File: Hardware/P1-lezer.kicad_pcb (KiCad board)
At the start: 2 copper layers, 70 x 30 mm, 13 parts, among them J1 RJ12, M2.5 MountingHole_2.7mm_M2.5_ISO73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, Q1 BC547, U1 WeMos_D1_mini, U2 TIL111

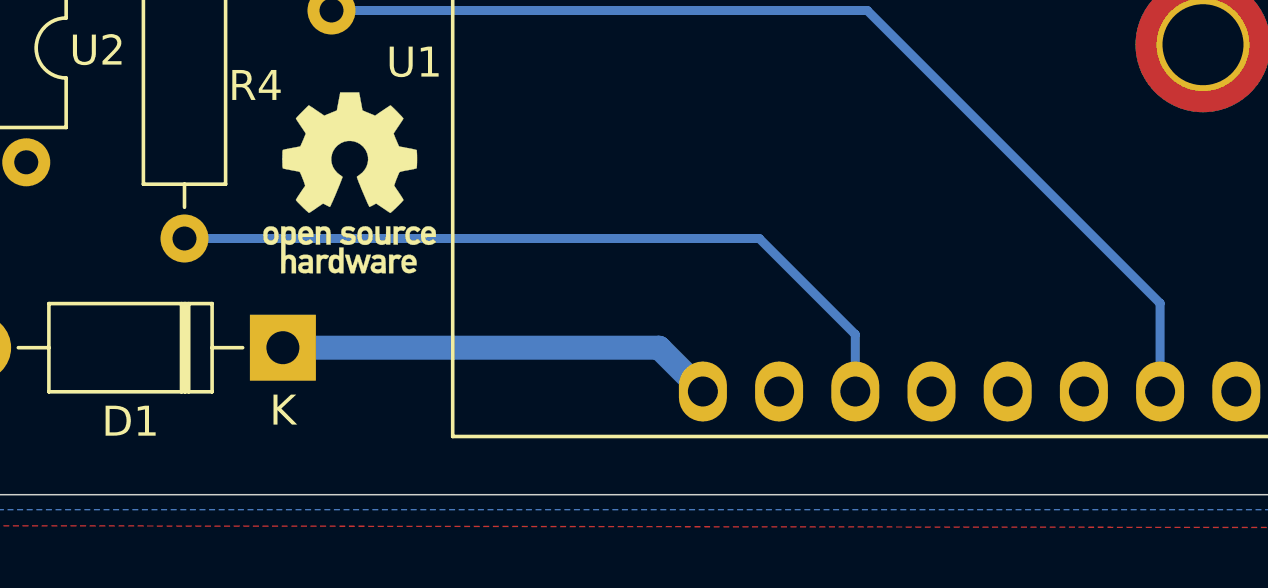
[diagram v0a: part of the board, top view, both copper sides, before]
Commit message: Moved request line to D1 and rerouted the board to match this change.
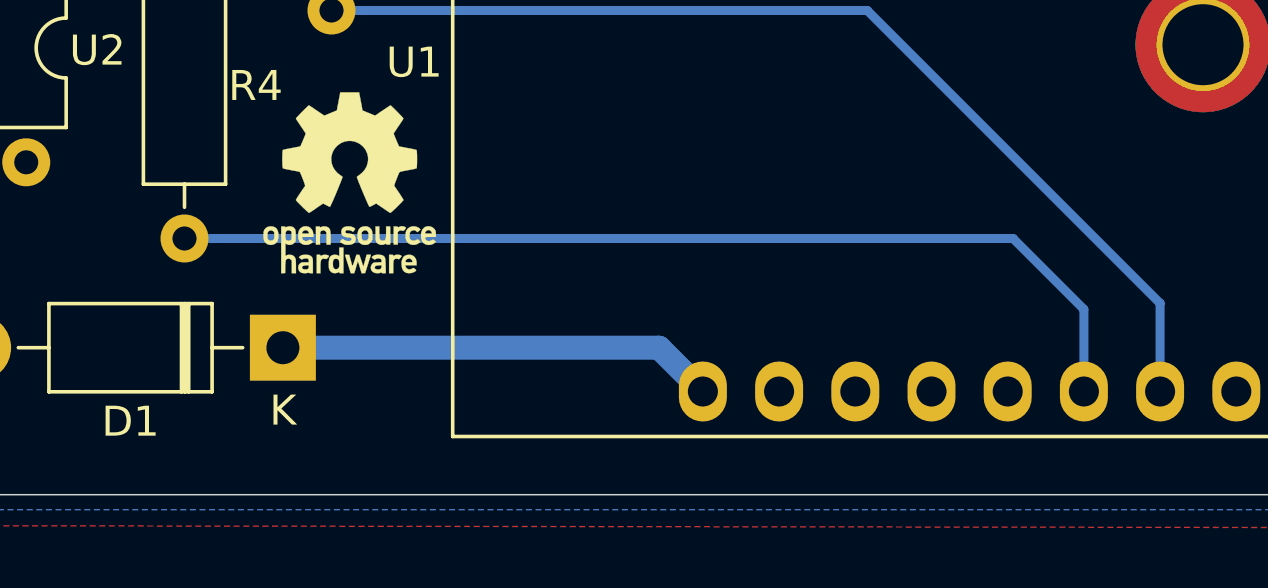
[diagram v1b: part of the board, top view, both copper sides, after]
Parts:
- R4: value 200 -> 220
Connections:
- U1 pad 11: Req -> unconnected-(U1-D4-Pad11)
- U1 pad 14: unconnected-(U1-SCL/D1-Pad14) -> Req
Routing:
- net Req: track 25.6 -> 33.7 mm
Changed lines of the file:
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@@
 	(net 15 "unconnected-(U1-D0-Pad3)")
 	(net 16 "unconnected-(U1-A0-Pad2)")
-	(net 17 "unconnected-(U1-SCL{slash}D1-Pad14)")
-	(net 18 "unconnected-(U1-SCK{slash}D5-Pad4)")
-	(net 19 "unconnected-(U1-CS{slash}D8-Pad7)")
-	(net 20 "unconnected-(U1-SDA{slash}D2-Pad13)")
-	(net 21 "unconnected-(J1-Pad4)")
-	(net 22 "unconnected-(U2-NC-Pad3)")
-	(net 23 "unconnected-(U2-Pad6)")
-	(net 24 "Net-(D1-K)")
+	(net 17 "unconnected-(U1-D4-Pad11)")
+	(net 18 "unconnected-(U1-CS{slash}D8-Pad7)")
+	(net 19 "unconnected-(U1-SDA{slash}D2-Pad13)")
+	(net 20 "unconnected-(J1-Pad4)")
+	(net 21 "unconnected-(U2-NC-Pad3)")
+	(net 22 "unconnected-(U2-Pad6)")
+	(net 23 "Net-(D1-K)")
+	(net 24 "unconnected-(U1-SCK{slash}D5-Pad4)")
 	(footprint "Symbol:OSHW-Logo_5.7x6mm_SilkScreen"
 		(layer "F.Cu")
@@
 			)
 		)
-		(property "Value" "200"
+		(property "Value" "220"
 			(at 5.08 2.37 90)
 			(layer "F.Fab")
@@
 			)
 		)
+		(property "Untitled Field" ""
+			(at 0 0 -90)
+			(unlocked yes)
+			(layer "F.Fab")
+			(hide yes)
+			(effects
+				(font
+					(size 1 1)
+					(thickness 0.15)
+				)
+			)
+		)
 		(property ki_fp_filters "R_*")
 		(sheetname "Root")
@@
 			(layers "*.Cu" "*.Mask")
 			(remove_unused_layers no)
-			(net 18 "unconnected-(U1-SCK{slash}D5-Pad4)")
+			(net 24 "unconnected-(U1-SCK{slash}D5-Pad4)")
 			(pinfunction "SCK/D5")
 			(pintype "bidirectional+no_connect")
@@
 			(layers "*.Cu" "*.Mask")
 			(remove_unused_layers no)
-			(net 19 "unconnected-(U1-CS{slash}D8-Pad7)")
+			(net 18 "unconnected-(U1-CS{slash}D8-Pad7)")
 			(pinfunction "CS/D8")
 			(pintype "bidirectional+no_connect")
@@
 			(layers "*.Cu" "*.Mask")
 			(remove_unused_layers no)
-			(net 24 "Net-(D1-K)")
+			(net 23 "Net-(D1-K)")
 			(pinfunction "5V")
 			(pintype "power_in")
@@
 			(layers "*.Cu" "*.Mask")
 			(remove_unused_layers no)
-			(net 7 "Req")
+			(net 17 "unconnected-(U1-D4-Pad11)")
 			(pinfunction "D4")
-			(pintype "bidirectional")
+			(pintype "bidirectional+no_connect")
 		)
 		(pad "12" thru_hole oval
@@
 			(layers "*.Cu" "*.Mask")
 			(remove_unused_layers no)
-			(net 20 "unconnected-(U1-SDA{slash}D2-Pad13)")
+			(net 19 "unconnected-(U1-SDA{slash}D2-Pad13)")
 			(pinfunction "SDA/D2")
 			(pintype "bidirectional+no_connect")
@@
 			(layers "*.Cu" "*.Mask")
 			(remove_unused_layers no)
-			(net 17 "unconnected-(U1-SCL{slash}D1-Pad14)")
+			(net 7 "Req")
 			(pinfunction "SCL/D1")
-			(pintype "bidirectional+no_connect")
+			(pintype "bidirectional")
 		)
 		(pad "15" thru_hole oval
@@
 			(layers "*.Cu" "*.Mask")
 			(remove_unused_layers no)
-			(net 21 "unconnected-(J1-Pad4)")
+			(net 20 "unconnected-(J1-Pad4)")
 			(pintype "passive+no_connect")
 		)
@@
 			(layers "*.Cu" "*.Mask")
 			(remove_unused_layers no)
-			(net 22 "unconnected-(U2-NC-Pad3)")
+			(net 21 "unconnected-(U2-NC-Pad3)")
 			(pinfunction "NC")
 			(pintype "no_connect")
@@
 			(layers "*.Cu" "*.Mask")
 			(remove_unused_layers no)
-			(net 23 "unconnected-(U2-Pad6)")
+			(net 22 "unconnected-(U2-Pad6)")
 			(pintype "passive+no_connect")
 		)
@@
 			(layers "*.Cu" "*.Mask")
 			(remove_unused_layers no)
-			(net 24 "Net-(D1-K)")
+			(net 23 "Net-(D1-K)")
 			(pinfunction "K")
 			(pintype "passive")
@@
 	)
 	(segment
-		(start 117.36 88.46)
-		(end 98.2 88.46)
+		(start 125.82 88.46)
+		(end 128.18 90.82)
 		(width 0.3)
 		(layer "B.Cu")
@@
 	)
 	(segment
-		(start 120.56 91.66)
-		(end 117.36 88.46)
+		(start 128.18 90.82)
+		(end 128.18 93.56)
 		(width 0.3)
 		(layer "B.Cu")
@@
 	)
 	(segment
-		(start 120.56 93.56)
-		(end 120.56 91.66)
+		(start 98.2 88.46)
+		(end 125.82 88.46)
 		(width 0.3)
 		(layer "B.Cu")
@@
 		(width 0.8)
 		(layer "B.Cu")
-		(net 24)
+		(net 23)
 	)
 	(segment
@@
 		(width 0.8)
 		(layer "B.Cu")
-		(net 24)
+		(net 23)
 	)
 	(zone

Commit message: Regenerated gerbers
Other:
- board text added: "Rev.B"
- board text removed: "Rev.A"
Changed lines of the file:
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@@
 		)
 	)
-	(gr_text "Rev.A"
+	(gr_text "Rev.B"
 		(at 75.2 94.6 0)
 		(layer "F.SilkS")

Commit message: Optocoupler aangepast naar CNY17-1
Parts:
- U2: value TIL111 -> CNY17-1
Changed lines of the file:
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@@
 				(font
 					(size 1.27 1.27)
+					(thickness 0.15)
 				)
 			)
@@
 				(font
 					(size 1.27 1.27)
+					(thickness 0.15)
 				)
 			)
@@
 				(font
 					(size 1.27 1.27)
+					(thickness 0.15)
 				)
 			)
@@
 				(font
 					(size 1.27 1.27)
+					(thickness 0.15)
 				)
 			)
@@
 				(font
 					(size 1.27 1.27)
+					(thickness 0.15)
 				)
 			)
@@
 				(font
 					(size 1.27 1.27)
+					(thickness 0.15)
 				)
 			)
@@
 				(font
 					(size 1.27 1.27)
+					(thickness 0.15)
 				)
 			)
@@
 				(font
 					(size 1.27 1.27)
+					(thickness 0.15)
 				)
 			)
@@
 				(font
 					(size 1.27 1.27)
+					(thickness 0.15)
 				)
 			)
@@
 				(font
 					(size 1.27 1.27)
+					(thickness 0.15)
 				)
 			)
@@
 				(font
 					(size 1.27 1.27)
+					(thickness 0.15)
 				)
 			)
@@
 				(font
 					(size 1.27 1.27)
+					(thickness 0.15)
 				)
 			)
@@
 				(font
 					(size 1.27 1.27)
+					(thickness 0.15)
 				)
 			)
@@
 				(font
 					(size 1.27 1.27)
+					(thickness 0.15)
 				)
 			)
@@
 				(font
 					(size 1.27 1.27)
+					(thickness 0.15)
 				)
 			)
@@
 				(font
 					(size 1.27 1.27)
+					(thickness 0.15)
 				)
 			)
@@
 				(font
 					(size 1.27 1.27)
+					(thickness 0.15)
 				)
 			)
@@
 				(font
 					(size 1.27 1.27)
+					(thickness 0.15)
 				)
 			)
@@
 				(font
 					(size 1.27 1.27)
+					(thickness 0.15)
 				)
 			)
@@
 				(font
 					(size 1.27 1.27)
+					(thickness 0.15)
 				)
 			)
@@
 				(font
 					(size 1.27 1.27)
+					(thickness 0.15)
 				)
 			)
@@
 				(font
 					(size 1.27 1.27)
+					(thickness 0.15)
 				)
 			)
@@
 				(font
 					(size 1.27 1.27)
+					(thickness 0.15)
 				)
 			)
@@
 				(font
 					(size 1.27 1.27)
+					(thickness 0.15)
 				)
 			)
@@
 				(font
 					(size 1.27 1.27)
+					(thickness 0.15)
 				)
 			)
@@
 				(font
 					(size 1.27 1.27)
+					(thickness 0.15)
 				)
 			)
@@
 				(font
 					(size 1.27 1.27)
+					(thickness 0.15)
 				)
 			)
@@
 			)
 		)
-		(property "Value" "TIL111"
+		(property "Value" "CNY17-1"
 			(at 3.81 7.41 90)
 			(layer "F.Fab")
@@
 				(font
 					(size 1.27 1.27)
+					(thickness 0.15)
 				)
 			)
 		)
-		(property "Datasheet" "https://www.egr.msu.edu/eceshop/Parts_Inventory/datasheets/til111.pdf"
+		(property "Datasheet" "http://www.vishay.com/docs/83606/cny17.pdf"
 			(at 0 0 -90)
 			(unlocked yes)
@@
 				(font
 					(size 1.27 1.27)
+					(thickness 0.15)
 				)
 			)
 		)
-		(property "Description" "DC Optocoupler, Phototransistor NPN, DIP6"
+		(property "Description" "DC Optocoupler Base Connected, Vce 70V, CTR 40-80%, Viso 5000V (RMS), DIP6"
 			(at 0 0 -90)
 			(unlocked yes)
@@
 				(font
 					(size 1.27 1.27)
+					(thickness 0.15)
 				)
 			)
 		)
-		(property ki_fp_filters "DIP*W7.62mm*")
+		(property "Untitled Field" ""
+			(at 0 0 -90)
+			(unlocked yes)
+			(layer "F.Fab")
+			(hide yes)
+			(effects
+				(font
+					(size 1 1)
+					(thickness 0.15)
+				)
+			)
+		)
+		(property ki_fp_filters "DIP*W7.62mm* DIP*W10.16mm* SMDIP*W9.53mm*")
 		(sheetname "Root")
 		(sheetfile "P1-lezer.kicad_sch")
@@
 				(font
 					(size 1.27 1.27)
+					(thickness 0.15)
 				)
 			)
@@
 				(font
 					(size 1.27 1.27)
+					(thickness 0.15)
 				)
 			)
@@
 				(font
 					(size 1.27 1.27)
+					(thickness 0.15)
 				)
 			)
@@
 				(font
 					(size 1.27 1.27)
+					(thickness 0.15)
 				)
 			)
@@
 				(font
 					(size 1.27 1.27)
+					(thickness 0.15)
 				)
 			)
@@
 				(font
 					(size 1.27 1.27)
+					(thickness 0.15)
 				)
 			)
@@
 				(font
 					(size 1.27 1.27)
+					(thickness 0.15)
 				)
 			)
@@
 				(font
 					(size 1.27 1.27)
+					(thickness 0.15)
 				)
 			)
@@
 				(font
 					(size 1.27 1.27)
+					(thickness 0.15)
 				)
 			)

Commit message: RST en +5V markering toegevoegd aan pcb om orientatie D1 Mini te verduidelijken.
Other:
- board text added: "+5V"
- board text added: "RST"
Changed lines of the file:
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@@
+		)
+	)
+	(gr_text "+5V"
+		(at 113.56 91.85 0)
+		(layer "F.SilkS")
+		(effects
+			(font
+				(size 1 1)
+				(thickness 0.153)
+			)
+			(justify left bottom)
+		)
+	)
+	(gr_text "RST"
+		(at 131.84 73.68 0)
+		(layer "F.SilkS")
+		(effects
+			(font
+				(size 1 1)
+				(thickness 0.153)
+			)
+			(justify left bottom)
 		)
 	)
